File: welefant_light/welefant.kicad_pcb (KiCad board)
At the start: 2 copper layers, 80 x 90 mm, 101 parts, among them J1 Conn_01x02, J2 Conn_02x8_Odd_Even, J3 Conn_02x6_Odd_Even, Q1 AO3401A, Q2 AO3401A, Q3 AO3401A, SW1 ON-OFF, SW2 RESET, SW3 BOOT, SW4 GPIO33, SW5 GPIO33, U1 RT9080-33GJ5, U2 Audio Jack PJ-324, U3 SD18OB261-060, U4 TP4056, U5 welefant, U6 128MBit Flash, U7 ESP32-S3, U8 Reset 2.8V, X1 40 MHz

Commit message: stand
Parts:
- SW5: value GPIO33 -> IO34
- U3: footprint easyeda2kicad:MIC-SMD_SD18OB261-060 -> hacrafu:MIC-SMD_SD18OB261-060
- moved SW5 65.6 mm to (105.0, 52.5)
- moved SW4 64.7 mm to (38.5, 52.5)
- moved U3 34.8 mm to (60.3, 54.1), turned to 90 degrees
- moved R4 30.8 mm to (46.2, 91.9)
- moved R6 30.4 mm to (44.9, 91.9)
- moved LED1 30.0 mm to (87.2, 83.0), turned to 180 degrees
- moved LED12 30.0 mm to (57.2, 93.0), turned to 180 degrees
- moved LED13 30.0 mm to (87.2, 98.0), turned to 180 degrees
- moved LED16 30.0 mm to (57.2, 98.0), turned to 180 degrees
- moved LED17 30.0 mm to (87.2, 103.0), turned to 180 degrees
- moved LED20 30.0 mm to (57.2, 103.0), turned to 180 degrees
- moved LED4 30.0 mm to (57.2, 83.0), turned to 180 degrees
- moved LED5 30.0 mm to (87.2, 88.0), turned to 180 degrees
- moved LED8 30.0 mm to (57.2, 88.0), turned to 180 degrees
- moved LED9 30.0 mm to (87.2, 93.0), turned to 180 degrees
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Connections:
- J2 pad 10: /BAT_SENS -> /MIC_CLK
- J2 pad 14: /AUDIO_PWM_R -> /USB_DP
- J2 pad 15: /USB_DN -> /AUDIO_PWM_R
- J2 pad 16: /USB_DP -> /USB_DN
- J2 pad 4: /TX -> /LED_HEAD
- J2 pad 5: /LED_HEAD -> /TX
- J2 pad 7: /MIC_CLK -> /BAT_SENS_EN
- J2 pad 9: /BAT_SENS_EN -> /BAT_SENS
- J3 pad 1: GND -> /VEXT
- J3 pad 4: /VEXT -> GND
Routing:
- net /VEXT: track 0.00 -> 285.2 mm, vias 0 -> 14
- net /V33: track 0.00 -> 135.6 mm, vias 0 -> 13
- net /TOUCH_T1: track 0.00 -> 131.7 mm, vias 0 -> 3
- net /TOUCH_T2: track 0.00 -> 124.6 mm, vias 0 -> 3
- net /TOUCH_T3: track 0.00 -> 117.0 mm, vias 0 -> 3
- net /TOUCH_T6: track 0.00 -> 91.8 mm, vias 0 -> 3
- net /TOUCH_T4: track 0.00 -> 90.3 mm, vias 0 -> 3
- net /TOUCH_T5: track 0.00 -> 87.5 mm, vias 0 -> 3
- net /USB_DP: track 0.00 -> 74.3 mm
- net /USB_DN: track 0.00 -> 71.9 mm
- net /LED_MATRIX: track 0.00 -> 60.2 mm, vias 0 -> 5
- net /BAT_SENS: track 0.00 -> 45.6 mm, vias 0 -> 4
- net /D1_LED: track 0.00 -> 45.2 mm
- net /D4_LED: track 0.00 -> 44.7 mm
- net /D3_LED: track 0.00 -> 44.6 mm
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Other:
- board text added: "IO33"
- board text added: "IO34"

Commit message: stand
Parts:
- added C24: 100n, easyeda2kicad:C0603, F.Cu at (60.3, 59.5)
- added C25: 1u, easyeda2kicad:C0603, F.Cu at (87.3, 107.1)
- J2: value Conn_02x8_Odd_Even -> Conn_02x7_Odd_Even; footprint hacrafu:PinHeader_2x08_P2.54mm_Vertical_SMD_handsolder -> hacrafu:PinHeader_2x07_P2.54mm_Vertical_SMD_handsolder
- moved Q1 25.1 mm to (65.6, 76.8), turned to 0 degrees
- moved R1 20.2 mm to (69.1, 76.2)
- moved R3 20.2 mm to (69.1, 77.8)
- moved R11 16.9 mm to (50.5, 88.1), turned to 0 degrees
- moved D1 14.5 mm to (61.3, 70.8)
- moved D2 11.7 mm to (63.8, 70.9)
- moved C20 9.53 mm to (68.3, 70.3), turned to 90 degrees
- moved C22 8.15 mm to (66.7, 70.3), turned to -90 degrees
- moved R19 7.70 mm to (44.2, 47.4), turned to 180 degrees
- moved C18 6.11 mm to (76.0, 51.8)
- moved R20 6.08 mm to (66.8, 59.8)
- moved L2 5.94 mm to (75.4, 49.7)
- moved C10 5.87 mm to (79.7, 56.2)
- moved C16 5.87 mm to (67.0, 55.8)
- moved R21 5.87 mm to (75.3, 63.5)
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- renumbered CLED1 to CRG
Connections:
- J2 pad 11: /JACK_SENS -> /AUDIO_PWM_R
- J2 pad 12: /LED -> /AUDIO_PWM_L
- J2 pad 13: /AUDIO_PWM_L -> /USB_DP
- J2 pad 14: /USB_DP -> /USB_DN
- J2 pad 4: /LED_HEAD -> /V5
- J2 pad 6: /LED_MATRIX -> /BAT_SENS
- J2 pad 9: /BAT_SENS -> /JACK_SENS
- USB1 pad 1: (no net) -> unconnected-(USB1-SH-Pad1)
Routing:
- net GND: track 18.7 -> 101.2 mm, vias 46 -> 458
- net /VBAT: track 43.3 -> 110.6 mm, vias 2 -> 6
- net /JACK_SENS: track 28.3 -> 89.6 mm
- net /VEXT_EN: track 37.2 -> 70.0 mm, vias 2 -> 6
- net /V5: track 43.8 -> 76.0 mm, vias 0 -> 4
- net /AUDIO_PWM_L: track 27.1 -> 57.9 mm, vias 2 -> 4
- net Net-(C4-Pad2): track 0.00 -> 28.6 mm, vias 0 -> 1
- net /AUDIO_PWM_R: track 29.3 -> 57.8 mm, vias 2 -> 4
- net /LED_HEAD: track 43.1 -> 17.7 mm, vias 5 -> 2
- net /LED_MATRIX: track 60.2 -> 35.7 mm, vias 5 -> 4
- net /V33: track 135.6 -> 113.3 mm, vias 13 -> 9
- net Net-(C5-Pad2): track 0.00 -> 20.7 mm, vias 0 -> 1
- net /LED: track 20.2 -> 3.14 mm, vias 4 -> 0
- net /BAT_SENS_EN: track 25.2 -> 40.8 mm
- net /GPIO34: track 33.7 -> 45.6 mm
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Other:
- outline, holes or cut-outs redrawn
- board text added: "BAT SE"
- board text added: "BAT SENS"
- board text added: "IO35"
- board text added: "IO36"
- board text added: "IO37"
- board text added: "IO38"
- board text added: "IO39"
- board text added: "IO40"
- board text added: "IO41"
- board text added: "IO42"
- board text added: "JACK SENS"
- board text added: "OFF"
- board text added: "ON"
- board text added: "V5 USB"
- board text removed: "35"
- board text removed: "36"
- board text removed: "37"
- board text removed: "38"
- board text removed: "39"
- board text removed: "40"
- board text removed: "41"
- board text removed: "42"
- board text removed: "BT SE"
- board text removed: "BT SENS"
- board text removed: "JCK S"
- board text removed: "LED"
- board text removed: "LED H"
- board text removed: "LED MATRIX"

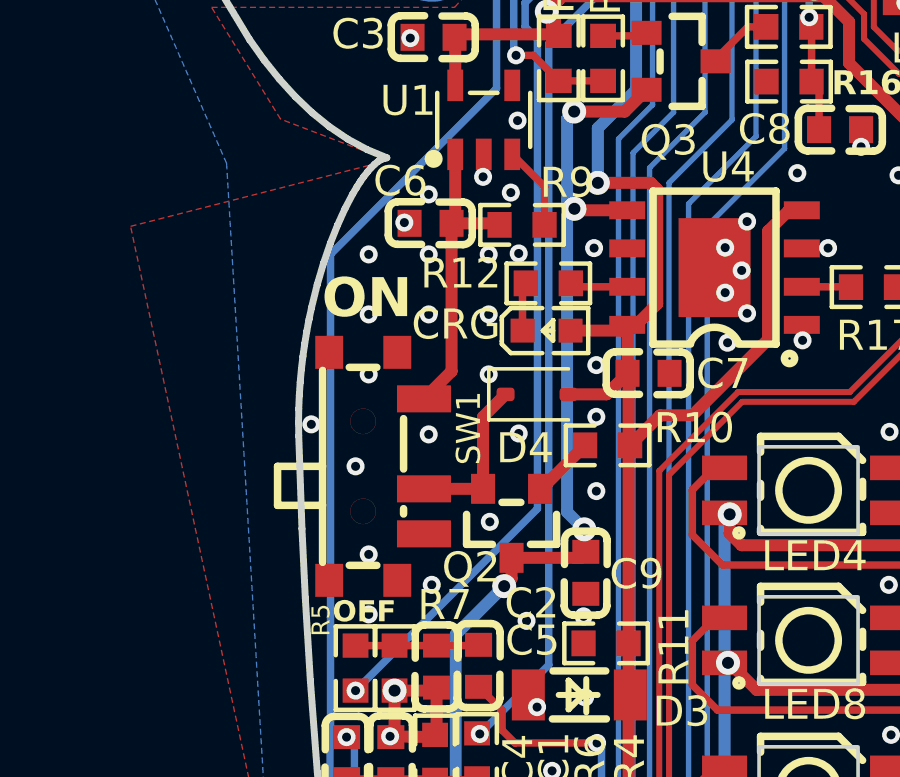
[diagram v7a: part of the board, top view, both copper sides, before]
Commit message: muss jetzt auf ESP32-S3FH4R2 umstellen
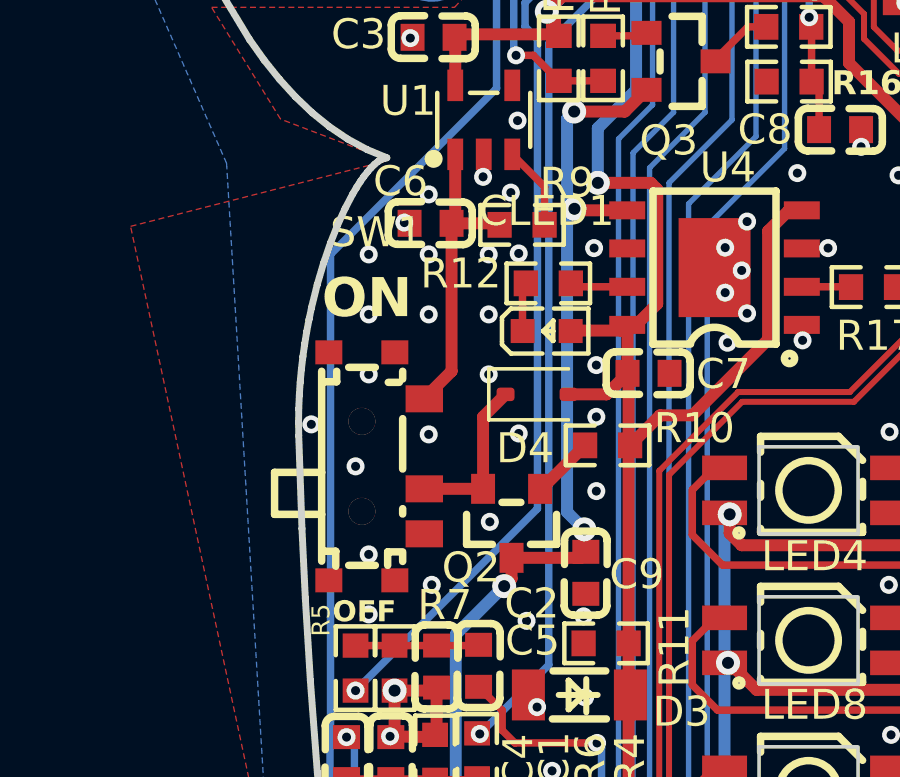
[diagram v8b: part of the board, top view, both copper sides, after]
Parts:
- removed CRG: yellow, easyeda2kicad:LED0603-RD-YELLOW
- added CLED1: yellow, easyeda2kicad:LED0603-RD-YELLOW, F.Cu at (48.5, 77.7)
- SW1: footprint easyeda2kicad:SW-SMD_MK-12C02-G025 -> easyeda2kicad:SW-TH_K3-1296S-E1
- turned SW1 to 0 degrees
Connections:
- SW1 pad 1: /VBUS -> unconnected-(SW1-Pad1)
- SW1 pad 3: unconnected-(SW1-Pad3) -> /VBUS
